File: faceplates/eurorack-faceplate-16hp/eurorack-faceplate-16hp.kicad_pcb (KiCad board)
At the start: 2 copper layers, 80.9 x 133.3 mm, 4 parts

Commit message: Moving mounting holes
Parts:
- moved REF** 2.42 mm to (5.08, 130.3)
- moved REF** 2.42 mm to (5.08, 3.00)
- moved REF** 2.28 mm to (75.8, 130.3)
- moved REF** 2.28 mm to (75.8, 3.00)
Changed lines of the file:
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@@
   (net 0 "")
   (footprint "MountingHole:MountingHole_3.2mm_M3" (layer "F.Cu")
-    (at 7.5 130.35)
+    (at 5.08 130.35)
     (descr "Mounting Hole 3.2mm, no annular, M3")
     (tags "mounting hole 3.2mm no annular m3")
@@
   )
   (footprint "MountingHole:MountingHole_3.2mm_M3" (layer "F.Cu")
-    (at 73.54 130.35)
+    (at 75.82 130.35)
     (descr "Mounting Hole 3.2mm, no annular, M3")
     (tags "mounting hole 3.2mm no annular m3")
@@
   )
   (footprint "MountingHole:MountingHole_3.2mm_M3" (layer "F.Cu")
-    (at 73.54 3)
+    (at 75.82 3)
     (descr "Mounting Hole 3.2mm, no annular, M3")
     (tags "mounting hole 3.2mm no annular m3")
@@
   )
   (footprint "MountingHole:MountingHole_3.2mm_M3" (layer "F.Cu")
-    (at 7.5 3)
+    (at 5.08 3)
     (descr "Mounting Hole 3.2mm, no annular, M3")
     (tags "mounting hole 3.2mm no annular m3")

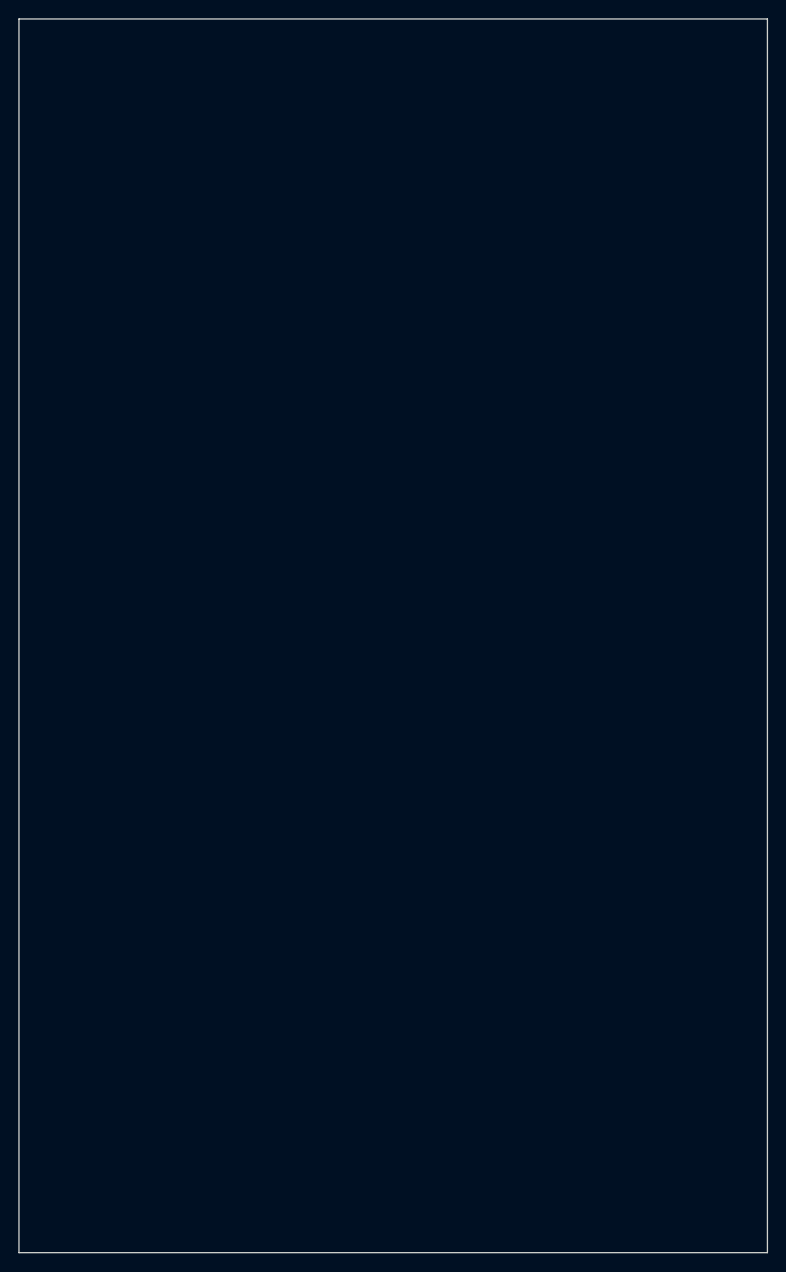
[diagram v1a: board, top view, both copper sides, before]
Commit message: Correcting panel height
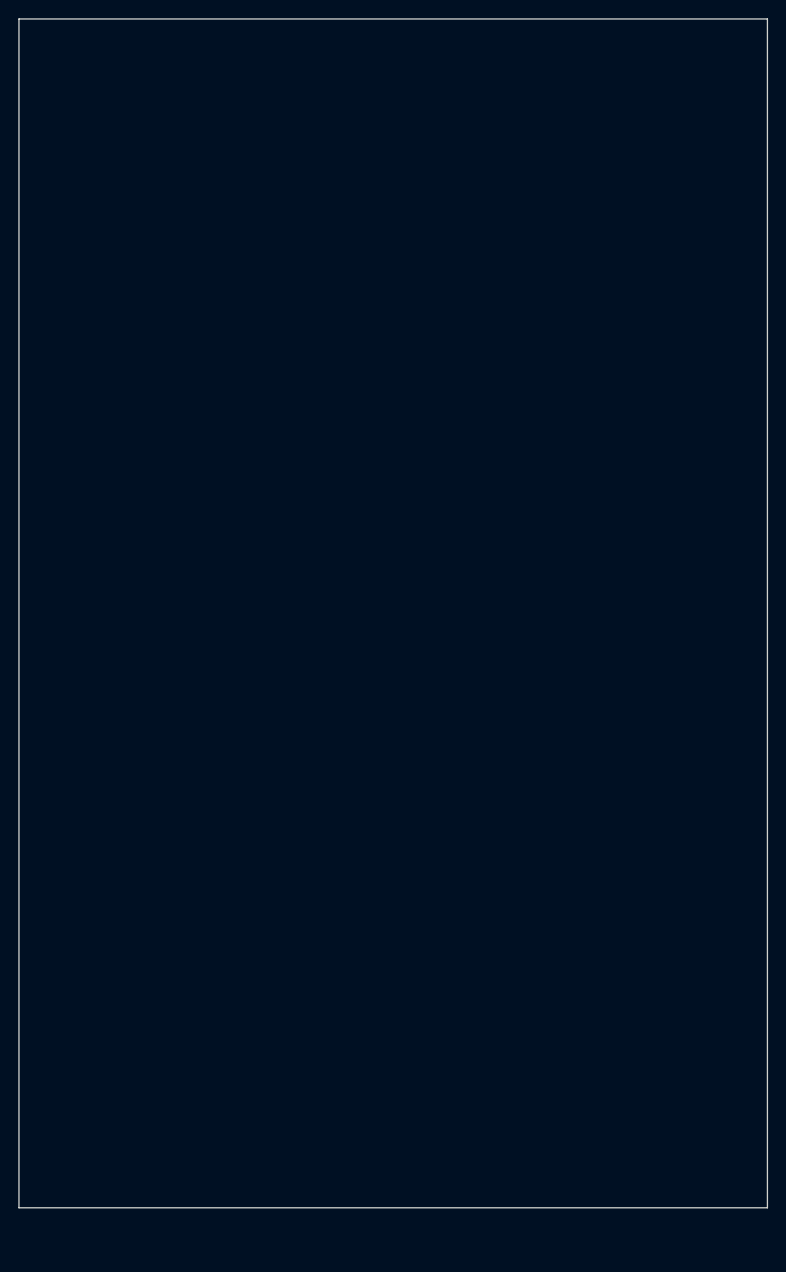
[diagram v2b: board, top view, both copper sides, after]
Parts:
- moved REF** 4.85 mm to (5.08, 125.5)
- moved REF** 4.85 mm to (75.8, 125.5)
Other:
- board size 80.9 x 133.3 mm -> 80.9 x 128.5 mm
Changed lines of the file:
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@@
   (net 0 "")
   (footprint "MountingHole:MountingHole_3.2mm_M3" (layer "F.Cu")
-    (at 5.08 130.35)
+    (at 5.08 125.5)
     (descr "Mounting Hole 3.2mm, no annular, M3")
     (tags "mounting hole 3.2mm no annular m3")
@@
   )
   (footprint "MountingHole:MountingHole_3.2mm_M3" (layer "F.Cu")
-    (at 75.82 130.35)
+    (at 75.82 125.5)
     (descr "Mounting Hole 3.2mm, no annular, M3")
     (tags "mounting hole 3.2mm no annular m3")
@@
     (pad "" np_thru_hole oval locked (at 0 0) (size 7 3.2) (drill oval 7 3.2) (layers F&B.Cu *.Mask))
   )
-  (gr_line (start 80.9 0) (end 80.9 133.35) (layer "Edge.Cuts") (width 0.1))
-  (gr_line (start 0 133.35) (end 0 0) (layer "Edge.Cuts") (width 0.1))
+  (gr_line (start 80.9 0) (end 80.9 128.5) (layer "Edge.Cuts") (width 0.1))
+  (gr_line (start 0 128.5) (end 0 0) (layer "Edge.Cuts") (width 0.1))
   (gr_line (start 0 0) (end 80.9 0) (layer "Edge.Cuts") (width 0.1))
-  (gr_line (start 80.9 133.35) (end 0 133.35) (layer "Edge.Cuts") (width 0.1))
+  (gr_line (start 80.9 128.5) (end 0 128.5) (layer "Edge.Cuts") (width 0.1))
 )
